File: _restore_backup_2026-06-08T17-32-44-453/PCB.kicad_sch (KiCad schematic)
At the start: 11 parts, among them J1 Conn_01x05_Pin, SW10 SW_Push, SW25 SW_DPST_x2, U1 STM32L010F4Px

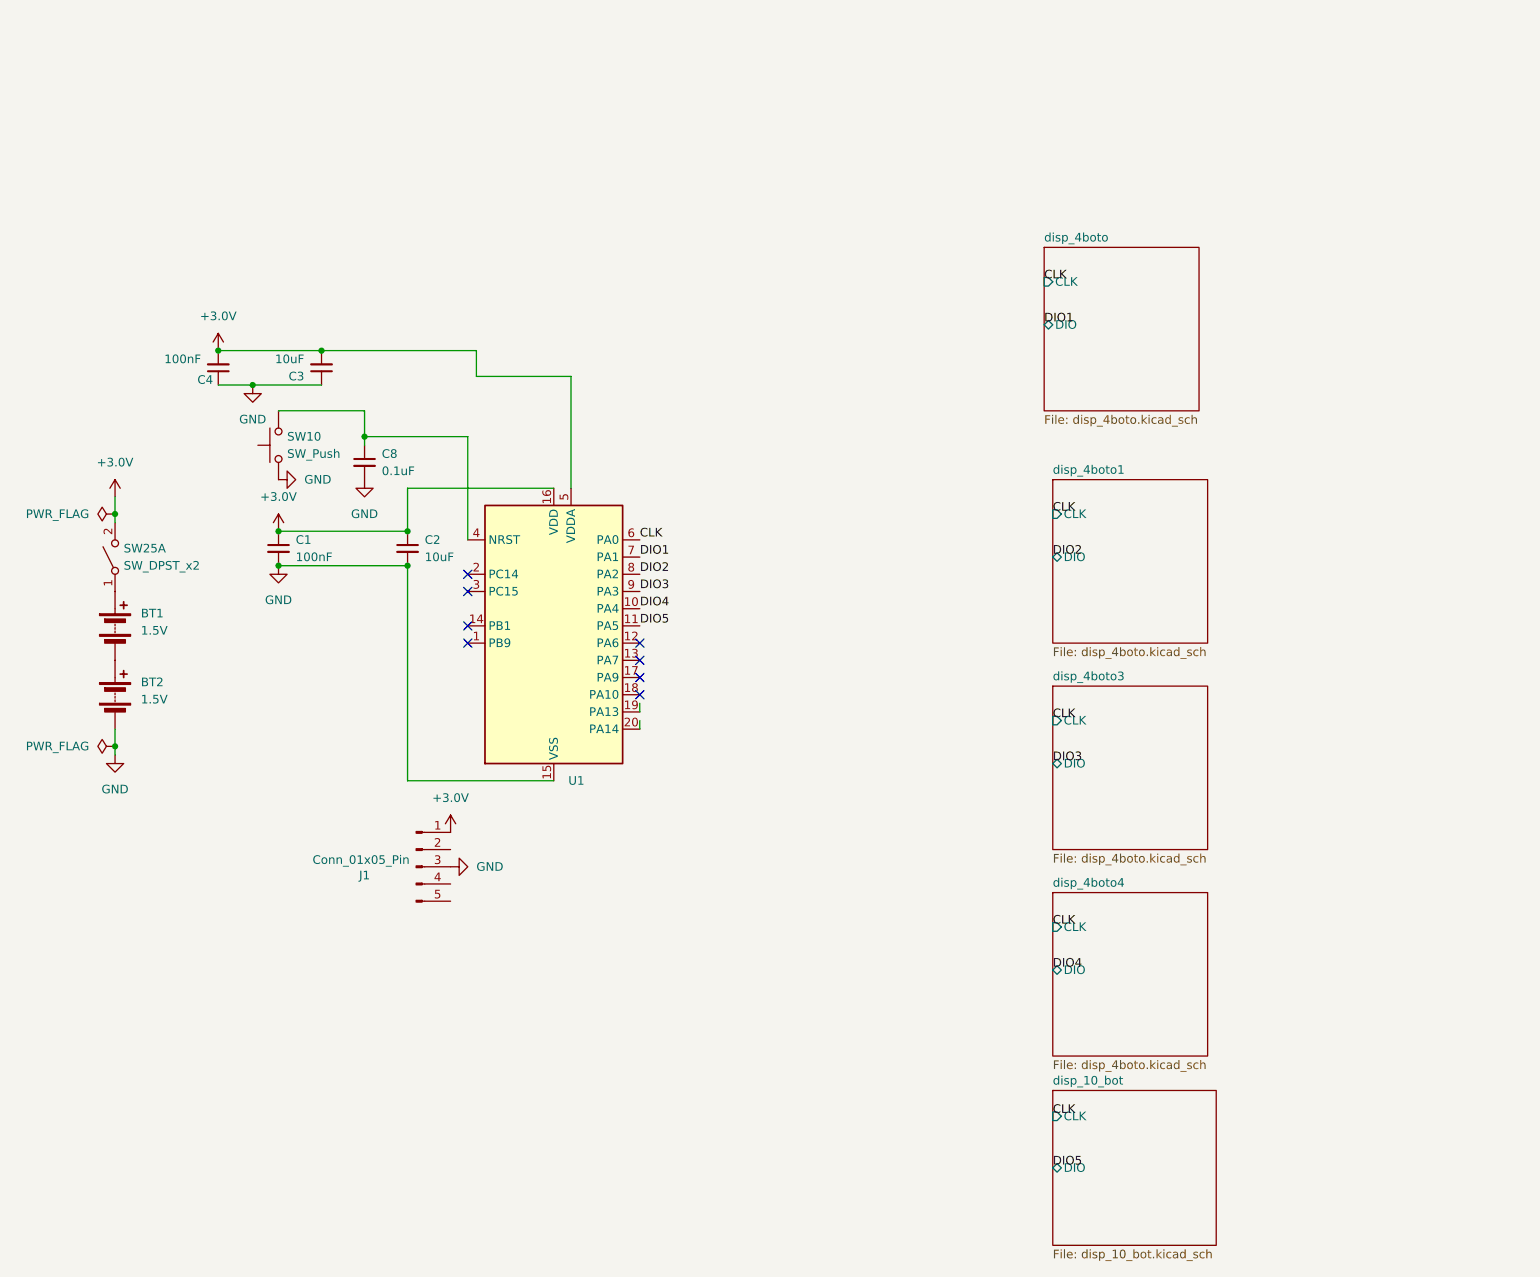
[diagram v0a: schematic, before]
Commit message: PCB Layout
Version finalizada del diseño del diseño de la PCB:
Se eliminaron los registros de 8 bits para dejar que los TM1637 manejen esa lógica y se metieron estos en hojas gerárquicas
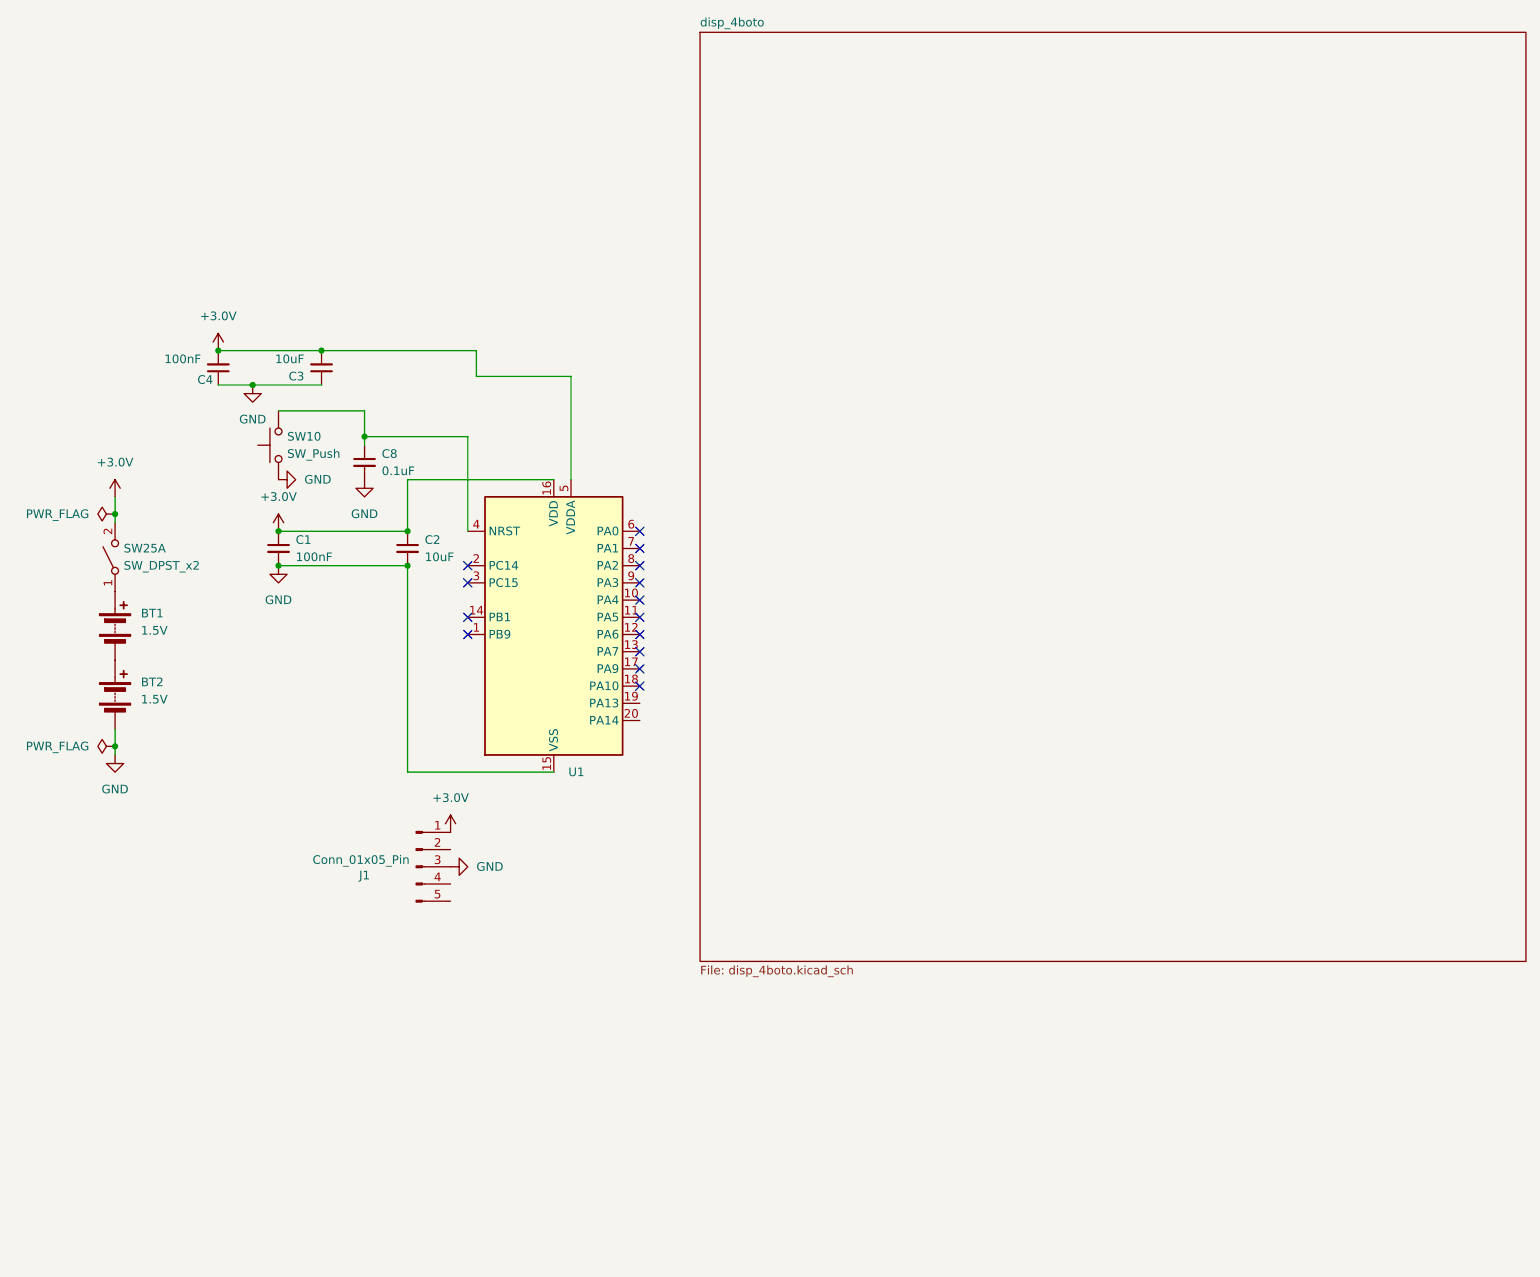
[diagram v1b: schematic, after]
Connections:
- net CLK: no longer names the net of U1.6 (PA0)
- net DIO1: no longer names the net of U1.7 (PA1)
- net DIO2: no longer names the net of U1.8 (PA2)
- net DIO3: no longer names the net of U1.9 (PA3)
- net DIO4: no longer names the net of U1.10 (PA4)
- net DIO5: no longer names the net of U1.11 (PA5)
- no-connect marks 8 -> 14
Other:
- removed sheet disp_10_bot
- removed sheet disp_4boto1
- removed sheet disp_4boto3
- removed sheet disp_4boto4
- sheet disp_4boto ports: added none; removed CLK, DIO
- moved on the sheet: U1
